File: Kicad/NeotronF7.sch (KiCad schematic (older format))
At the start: 58 parts, among them J1 Conn_02x05_Odd_Even, J2 USB_B_Micro, J3 DB9_Male_MountingHoles, J4 ATAPI Interface 1, J5 SD_Card, J6 SD_Card, J7 ATAPI Interface 2, J8 Double-mini-DIN-6, U1 AMS1117-3.3, U2 STM32F767BGTx, U5 MAX232, X1 50MHz XO, Y1 16 MHz, Y2 32.768 kHz

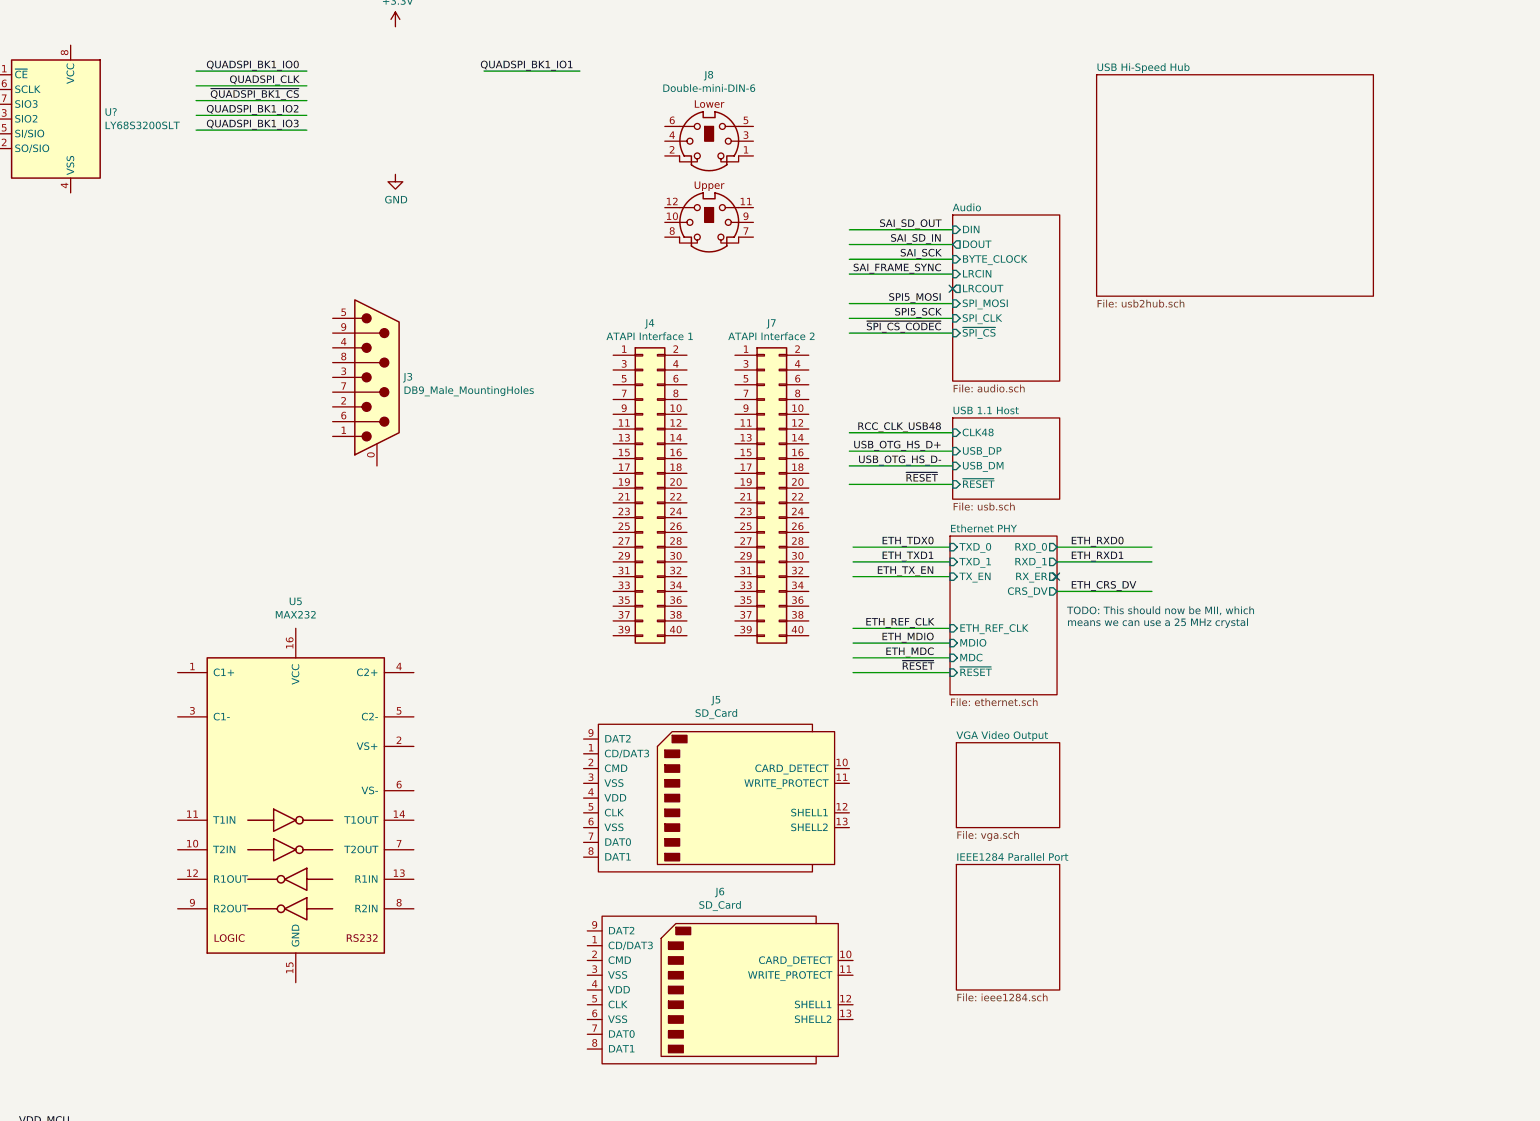
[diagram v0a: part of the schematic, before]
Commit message: Adding VGA output buffer/filter.
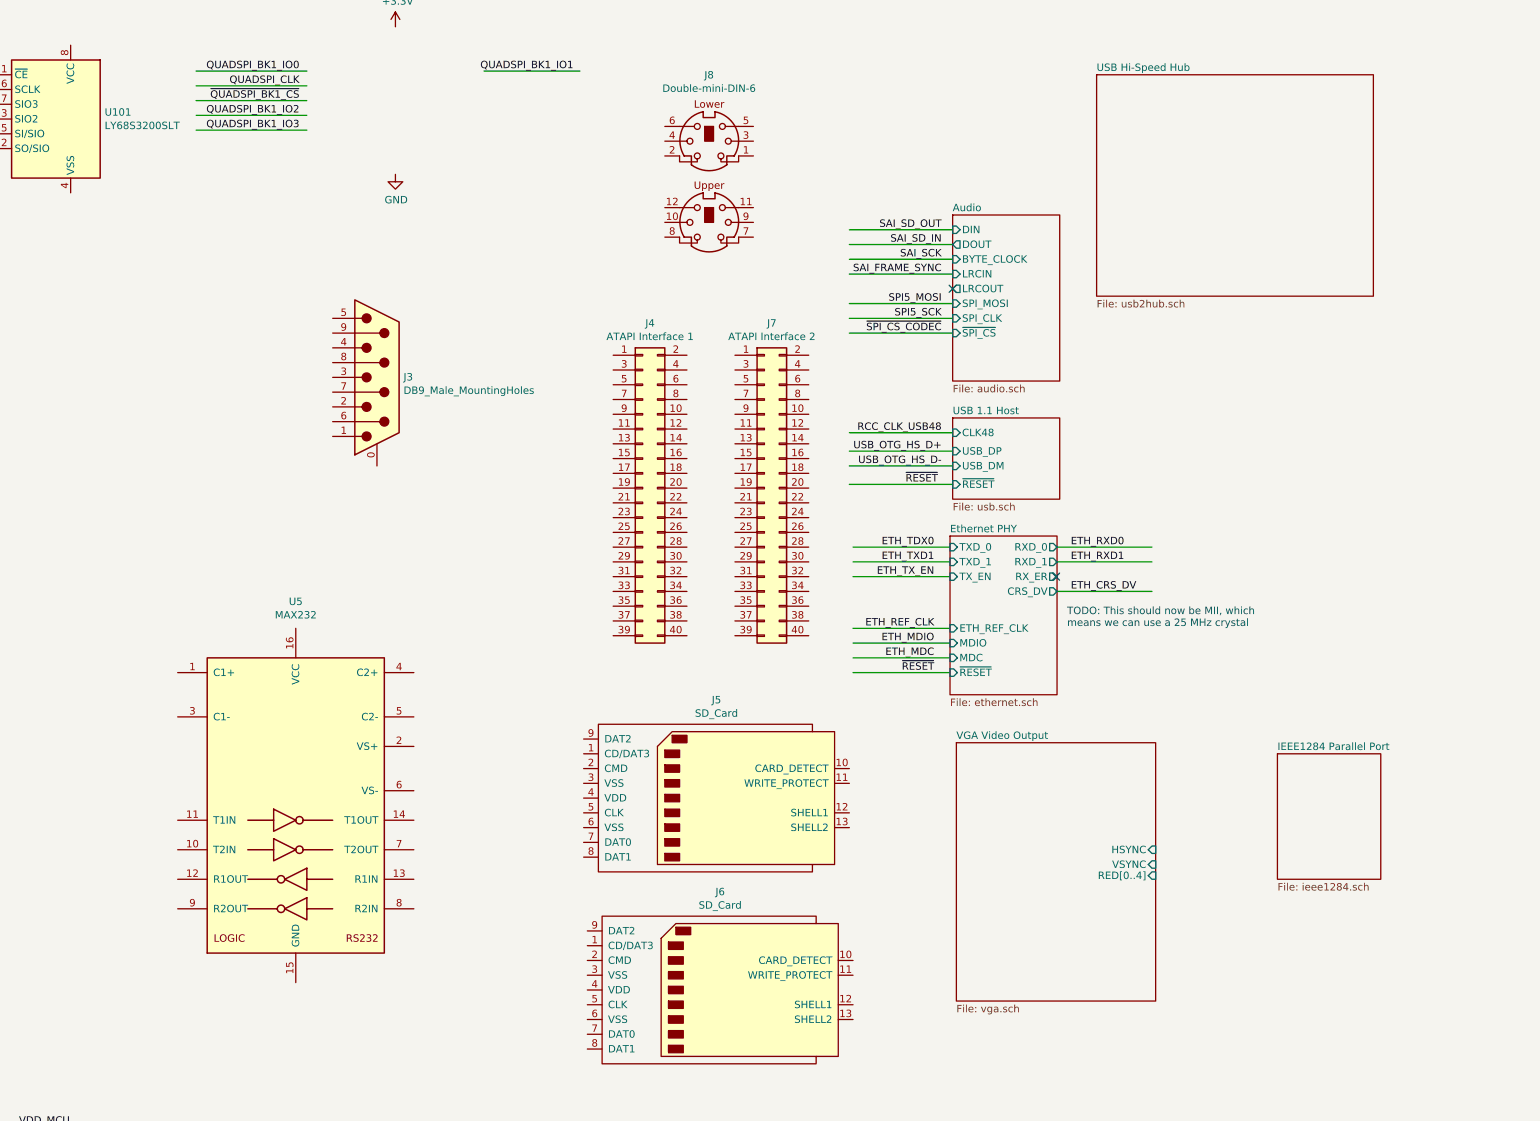
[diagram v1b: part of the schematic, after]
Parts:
- gave numbers to parts that had none: 1
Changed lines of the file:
@@
 $EndSheet
 $Sheet
-S 14700 9625 700  850
+S 16875 8875 700  850
 U 5EF25502
 F0 "IEEE1284 Parallel Port" 50
 F1 "ieee1284.sch" 50
-$EndSheet
-$Sheet
-S 14700 8800 700  575
-U 5EF2A2A2
-F0 "VGA Video Output" 50
-F1 "vga.sch" 50
 $EndSheet
 $Comp
@@
 	-7575 9550 -7475 9650
 $Comp
-L Memory_RAM:ESP-PSRAM32 U?
+L Memory_RAM:ESP-PSRAM32 U101
 U 1 1 6438446A
 P 8600 4575
-F 0 "U?" H 8270 4621 50  0000 R CNN
+F 0 "U101" H 8270 4621 50  0000 R CNN
 F 1 "LY68S3200SLT" H 8270 4530 50  0000 R CNN
 F 2 "Package_SO:SOIC-8_3.9x4.9mm_P1.27mm" H 8600 3975 50  0001 C CNN
@@
 Wire Bus Line
 	-7475 7375 -7475 11175
+$Sheet
+S 14700 8800 1350 1750
+U 5EF2A2A2
+F0 "VGA Video Output" 50
+F1 "vga.sch" 50
+F2 "HSYNC" I R 16050 9525 50
+F3 "VSYNC" I R 16050 9625 50
+F4 "RED[0..4]" I R 16050 9700 50
+$EndSheet
 $EndSCHEMATC
